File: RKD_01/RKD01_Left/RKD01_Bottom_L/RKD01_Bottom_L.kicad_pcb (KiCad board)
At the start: 2 copper layers, 164.3 x 126.2 mm, 8 parts

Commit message: 寸法を見直し
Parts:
- M1, M2, M3, M4, M5, M6, M7, M8: renamed from Ref**; value Val** -> Mark
- moved M7 21.4 mm to (26.2, 140.5)
- moved M8 4.76 mm to (185.7, 140.5)
- moved M2 4.76 mm to (185.7, 23.8)
- moved M4 2.38 mm to (135.7, 47.6)
- moved M6 2.38 mm to (135.7, 104.8)
- moved M3 2.38 mm to (31.0, 47.6)
- moved M5 2.38 mm to (73.8, 85.7)
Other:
- board size 164.3 x 126.2 mm -> 169.1 x 126.2 mm
- board text added: "RKD01_Left v1.0"
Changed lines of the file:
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@@
 			(drillshape 0)
 			(scaleselection 1)
-			(outputdirectory "../../../../Order/20241231/RKD01/Bottom_L/")
+			(outputdirectory "../../../../Order/20241231/RKD01/Assemble_L/")
 		)
 	)
@@
 	(footprint "kbd_Hole:m2_Screw_Hole"
 		(layer "F.Cu")
-		(at 133.35 104.775)
+		(at 135.7313 104.775)
 		(descr "Mounting Hole 2.2mm, no annular, M2")
 		(tags "mounting hole 2.2mm no annular m2")
-		(property "Reference" "Ref**"
+		(property "Reference" "M6"
 			(at 0 -3.2 0)
 			(layer "F.Fab")
@@
 			)
 		)
-		(property "Value" "Val**"
+		(property "Value" "Mark"
 			(at 0 3.2 0)
 			(layer "F.Fab")
@@
 			)
 		)
+		(sheetname "ルート")
+		(sheetfile "RKD01_Assemble_L.kicad_sch")
 		(attr exclude_from_pos_files exclude_from_bom)
 		(fp_circle
@@
 	(footprint "kbd_Hole:m2_Screw_Hole"
 		(layer "F.Cu")
-		(at 71.4375 85.725)
+		(at 73.8188 85.725)
 		(descr "Mounting Hole 2.2mm, no annular, M2")
 		(tags "mounting hole 2.2mm no annular m2")
-		(property "Reference" "Ref**"
+		(property "Reference" "M5"
 			(at 0 -3.2 0)
 			(layer "F.Fab")
@@
 			)
 		)
-		(property "Value" "Val**"
+		(property "Value" "Mark"
 			(at 0 3.2 0)
 			(layer "F.Fab")
@@
 			)
 		)
+		(sheetname "ルート")
+		(sheetfile "RKD01_Assemble_L.kicad_sch")
 		(attr exclude_from_pos_files exclude_from_bom)
 		(fp_circle
@@
 	(footprint "kbd_Hole:m2_Screw_Hole"
 		(layer "F.Cu")
-		(at 180.975 23.8125)
+		(at 185.7375 23.8125)
 		(descr "Mounting Hole 2.2mm, no annular, M2")
 		(tags "mounting hole 2.2mm no annular m2")
-		(property "Reference" "Ref**"
+		(property "Reference" "M2"
 			(at 0 -3.2 0)
 			(layer "F.Fab")
@@
 			)
 		)
-		(property "Value" "Val**"
+		(property "Value" "Mark"
 			(at 0 3.2 0)
 			(layer "F.Fab")
@@
 			)
 		)
+		(sheetname "ルート")
+		(sheetfile "RKD01_Assemble_L.kicad_sch")
 		(attr exclude_from_pos_files exclude_from_bom)
 		(fp_circle
@@
 	(footprint "kbd_Hole:m2_Screw_Hole"
 		(layer "F.Cu")
-		(at 180.975 140.49375)
+		(at 185.7375 140.4937)
 		(descr "Mounting Hole 2.2mm, no annular, M2")
 		(tags "mounting hole 2.2mm no annular m2")
-		(property "Reference" "Ref**"
+		(property "Reference" "M8"
 			(at 0 -3.2 0)
 			(layer "F.Fab")
@@
 			)
 		)
-		(property "Value" "Val**"
+		(property "Value" "Mark"
 			(at 0 3.2 0)
 			(layer "F.Fab")
@@
 			)
 		)
+		(sheetname "ルート")
+		(sheetfile "RKD01_Assemble_L.kicad_sch")
 		(attr exclude_from_pos_files exclude_from_bom)
 		(fp_circle
@@
 	(footprint "kbd_Hole:m2_Screw_Hole"
 		(layer "F.Cu")
-		(at 47.625 140.49375)
+		(at 26.1938 140.4937)
 		(descr "Mounting Hole 2.2mm, no annular, M2")
 		(tags "mounting hole 2.2mm no annular m2")
-		(property "Reference" "Ref**"
+		(property "Reference" "M7"
 			(at 0 -3.2 0)
 			(layer "F.Fab")
@@
 			)
 		)
-		(property "Value" "Val**"
+		(property "Value" "Mark"
 			(at 0 3.2 0)
 			(layer "F.Fab")
@@
 			)
 		)
+		(sheetname "ルート")
+		(sheetfile "RKD01_Assemble_L.kicad_sch")
 		(attr exclude_from_pos_files exclude_from_bom)
 		(fp_circle
@@
 	(footprint "kbd_Hole:m2_Screw_Hole"
 		(layer "F.Cu")
-		(at 88.10625 23.8125)
+		(at 88.1063 23.8125)
 		(descr "Mounting Hole 2.2mm, no annular, M2")
 		(tags "mounting hole 2.2mm no annular m2")
-		(property "Reference" "Ref**"
+		(property "Reference" "M1"
 			(at 0 -3.2 0)
 			(layer "F.Fab")
@@
 			)
 		)
-		(property "Value" "Val**"
+		(property "Value" "Mark"
 			(at 0 3.2 0)
 			(layer "F.Fab")
@@
 			)
 		)
+		(sheetname "ルート")
+		(sheetfile "RKD01_Assemble_L.kicad_sch")
 		(attr exclude_from_pos_files exclude_from_bom)
 		(fp_circle
@@
 	(footprint "kbd_Hole:m2_Screw_Hole"
 		(layer "F.Cu")
-		(at 133.35 47.625)
+		(at 135.7313 47.625)
 		(descr "Mounting Hole 2.2mm, no annular, M2")
 		(tags "mounting hole 2.2mm no annular m2")
-		(property "Reference" "Ref**"
+		(property "Reference" "M4"
 			(at 0 -3.2 0)
 			(layer "F.Fab")
@@
 			)
 		)
-		(property "Value" "Val**"
+		(property "Value" "Mark"
 			(at 0 3.2 0)
 			(layer "F.Fab")
@@
 			)
 		)
+		(sheetname "ルート")
+		(sheetfile "RKD01_Assemble_L.kicad_sch")
 		(attr exclude_from_pos_files exclude_from_bom)
 		(fp_circle
@@
 	(footprint "kbd_Hole:m2_Screw_Hole"
 		(layer "F.Cu")
-		(at 28.575 47.625)
+		(at 30.9563 47.625)
 		(descr "Mounting Hole 2.2mm, no annular, M2")
 		(tags "mounting hole 2.2mm no annular m2")
-		(property "Reference" "Ref**"
+		(property "Reference" "M3"
 			(at 0 -3.2 0)
 			(layer "F.Fab")
@@
 			)
 		)
-		(property "Value" "Val**"
+		(property "Value" "Mark"
 			(at 0 3.2 0)
 			(layer "F.Fab")
@@
 			)
 		)
+		(sheetname "ルート")
+		(sheetfile "RKD01_Assemble_L.kicad_sch")
 		(attr exclude_from_pos_files exclude_from_bom)
 		(fp_circle
@@
 	)
 	(gr_arc
-		(start 183.35625 19.05)
-		(mid 185.040048 19.747452)
-		(end 185.7375 21.43125)
+		(start 188.1188 19.04995)
+		(mid 189.802583 19.747417)
+		(end 190.50005 21.4312)
 		(stroke
 			(width 0.05)
@@
 	)
 	(gr_line
-		(start 183.35625 19.05)
+		(start 188.1188 19.04995)
 		(end 23.8125 19.05)
 		(stroke
@@
 	)
 	(gr_arc
-		(start 21.43125 21.43125)
-		(mid 22.128702 19.747452)
-		(end 23.8125 19.05)
+		(start 21.43125 21.4313)
+		(mid 22.128702 19.747502)
+		(end 23.8125 19.05005)
 		(stroke
 			(width 0.05)
@@
 	)
 	(gr_arc
-		(start 185.7375 142.875)
-		(mid 185.040048 144.558798)
-		(end 183.35625 145.25625)
+		(start 190.50005 142.875)
+		(mid 189.802601 144.558816)
+		(end 188.1188 145.25625)
 		(stroke
 			(width 0.05)
@@
 	(gr_line
 		(start 23.8125 145.25625)
-		(end 183.35625 145.25625)
+		(end 188.1188 145.25625)
 		(stroke
 			(width 0.05)
@@
 	)
 	(gr_line
-		(start 185.7375 142.875)
-		(end 185.7375 21.43125)
+		(start 190.5 142.875)
+		(end 190.5 21.43125)
 		(stroke
 			(width 0.05)
@@
 		(layer "Edge.Cuts")
 	)
+	(gr_text "RKD01_Left v1.0"
+		(at 176.2125 23.8125 0)
+		(layer "B.SilkS")
+		(effects
+			(font
+				(size 1 1)
+				(thickness 0.1)
+			)
+			(justify left bottom mirror)
+		)
+	)
 )

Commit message: デザイン見直し
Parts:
- removed M7, M8: Mark, kbd_Hole:m2_Screw_Hole
- moved M4 109.0 mm to (192.9, 140.5)
- moved M3 93.0 mm to (26.2, 140.5)
- moved M6 89.6 mm to (78.6, 35.7)
- moved M5 59.7 mm to (78.6, 26.2)
- moved M2 7.14 mm to (192.9, 23.8)
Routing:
- net Row4: track 0.00 -> 2.03 mm
- net Net-(D5-A): track 0.00 -> 2.03 mm
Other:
- board size 169.1 x 126.2 mm -> 176.2 x 126.2 mm

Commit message: デザイン見直し
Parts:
- added M7: Mark, kbd_Hole:m2_Screw_Hole, F.Cu at (23.8, 47.6)
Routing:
- net Row4: track 2.03 -> 0.00 mm
- net Net-(D5-A): track 2.03 -> 0.00 mm
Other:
- outline, holes or cut-outs redrawn
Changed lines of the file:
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@@
 	)
 	(net 0 "")
-	(net 1 "Row4")
-	(net 2 "Net-(D5-A)")
 	(footprint "kbd_Hole:m2_Screw_Hole"
 		(layer "F.Cu")
@@
 	(footprint "kbd_Hole:m2_Screw_Hole"
 		(layer "F.Cu")
+		(at 23.8125 47.625)
+		(descr "Mounting Hole 2.2mm, no annular, M2")
+		(tags "mounting hole 2.2mm no annular m2")
+		(property "Reference" "M7"
+			(at 0 -3.2 0)
+			(layer "F.Fab")
+			(effects
+				(font
+					(size 1 1)
+					(thickness 0.15)
+				)
+			)
+		)
+		(property "Value" "Mark"
+			(at 0 3.2 0)
+			(layer "F.Fab")
+			(effects
+				(font
+					(size 1 1)
+					(thickness 0.15)
+				)
+			)
+		)
+		(property "Footprint" "kbd_Hole:m2_Screw_Hole"
+			(at 0 0 0)
+			(layer "F.Fab")
+			(hide yes)
+			(effects
+				(font
+					(size 1.27 1.27)
+					(thickness 0.15)
+				)
+			)
+		)
+		(property "Datasheet" ""
+			(at 0 0 0)
+			(layer "F.Fab")
+			(hide yes)
+			(effects
+				(font
+					(size 1.27 1.27)
+					(thickness 0.15)
+				)
+			)
+		)
+		(property "Description" ""
+			(at 0 0 0)
+			(layer "F.Fab")
+			(hide yes)
+			(effects
+				(font
+					(size 1.27 1.27)
+					(thickness 0.15)
+				)
+			)
+		)
+		(attr exclude_from_pos_files)
+		(fp_circle
+			(center 0 0)
+			(end 2.2 0)
+			(stroke
+				(width 0.15)
+				(type solid)
+			)
+			(fill none)
+			(layer "Cmts.User")
+		)
+		(fp_circle
+			(center 0 0)
+			(end 2.45 0)
+			(stroke
+				(width 0.05)
+				(type solid)
+			)
+			(fill none)
+			(layer "F.CrtYd")
+		)
+		(fp_text user "${REFERENCE}"
+			(at 0.3 0 0)
+			(layer "F.Fab")
+			(effects
+				(font
+					(size 1 1)
+					(thickness 0.15)
+				)
+			)
+		)
+		(pad "" np_thru_hole circle
+			(at 0 0)
+			(size 2.2 2.2)
+			(drill 2.2)
+			(layers "*.Cu" "*.Mask")
+		)
+	)
+	(footprint "kbd_Hole:m2_Screw_Hole"
+		(layer "F.Cu")
 		(at 26.1938 140.4937)
 		(descr "Mounting Hole 2.2mm, no annular, M2")
@@
 		)
 	)
-	(gr_arc
-		(start 195.26255 19.0499)
-		(mid 196.946319 19.747381)
-		(end 197.6438 21.43115)
+	(gr_line
+		(start 196.453125 19.05)
+		(end 22.621875 19.05)
 		(stroke
 			(width 0.05)
@@
 		(layer "Edge.Cuts")
 	)
-	(gr_line
-		(start 195.26255 19.0499)
-		(end 23.81245 19.05005)
+	(gr_arc
+		(start 22.621875 145.25625)
+		(mid 21.779976 144.907524)
+		(end 21.43125 144.065625)
 		(stroke
 			(width 0.05)
@@
 	)
 	(gr_arc
-		(start 21.4312 21.4313)
-		(mid 22.128652 19.747502)
-		(end 23.81245 19.05005)
+		(start 196.453125 19.05)
+		(mid 197.295024 19.398726)
+		(end 197.64375 20.240625)
 		(stroke
 			(width 0.05)
@@
 	)
 	(gr_arc
-		(start 197.6437 142.875)
-		(mid 196.946248 144.558798)
-		(end 195.26245 145.25625)
+		(start 197.64375 144.065625)
+		(mid 197.295024 144.907524)
+		(end 196.453125 145.25625)
 		(stroke
 			(width 0.05)
@@
 	)
 	(gr_arc
-		(start 23.8125 145.25625)
-		(mid 22.128702 144.558798)
-		(end 21.43125 142.875)
+		(start 21.43125 20.240625)
+		(mid 21.779976 19.398726)
+		(end 22.621875 19.05)
 		(stroke
 			(width 0.05)
@@
 	)
 	(gr_line
-		(start 23.8125 145.25625)
-		(end 195.26245 145.25625)
+		(start 22.621875 145.25625)
+		(end 196.453125 145.25625)
 		(stroke
 			(width 0.05)
@@
 	)
 	(gr_line
-		(start 197.6437 142.875)
-		(end 197.6437 21.43125)
+		(start 197.64375 144.065625)
+		(end 197.64375 20.240625)
 		(stroke
 			(width 0.05)
@@
 	)
 	(gr_line
-		(start 21.43125 142.875)
-		(end 21.43125 21.43125)
+		(start 21.43125 144.065625)
+		(end 21.43125 20.240625)
 		(stroke
 			(width 0.05)
@@
 		)
 	)
-	(segment
-		(start 33.3376 126.8125)
-		(end 33.3376 124.7775)
-		(width 0.25)
-		(layer "B.Cu")
-		(net 1)
-	)
-	(segment
-		(start 33.3376 132.3975)
-		(end 33.3376 130.3625)
-		(width 0.25)
-		(layer "B.Cu")
-		(net 2)
-	)
 )

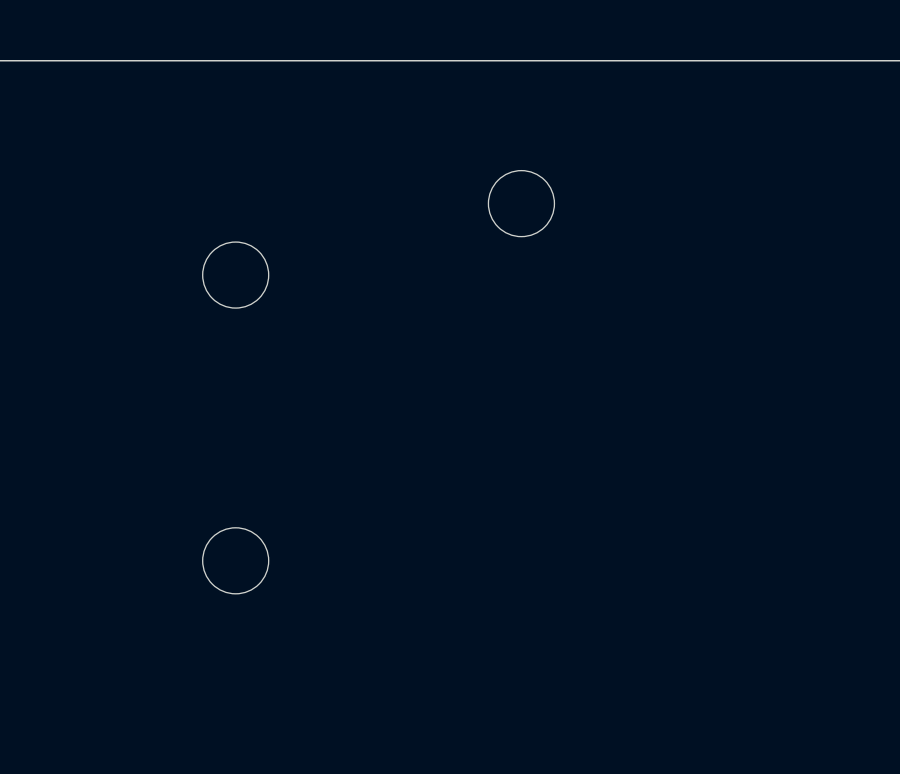
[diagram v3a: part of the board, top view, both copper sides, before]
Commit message: promicro部分拡張
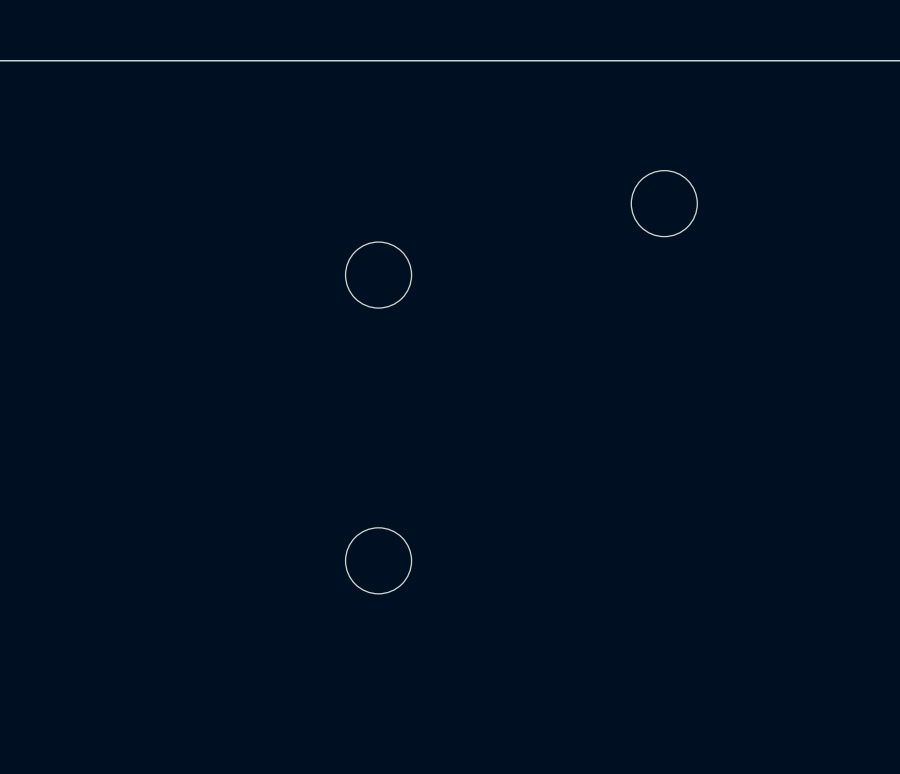
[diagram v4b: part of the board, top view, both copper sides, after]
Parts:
- moved M1 4.76 mm to (92.9, 23.8)
- moved M5 4.76 mm to (83.3, 26.2)
- moved M6 4.76 mm to (83.3, 35.7)
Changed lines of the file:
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@@
 	(footprint "kbd_Hole:m2_Screw_Hole"
 		(layer "F.Cu")
-		(at 78.5813 26.1937)
+		(at 83.34375 26.1937)
 		(descr "Mounting Hole 2.2mm, no annular, M2")
 		(tags "mounting hole 2.2mm no annular m2")
@@
 	(footprint "kbd_Hole:m2_Screw_Hole"
 		(layer "F.Cu")
-		(at 78.5813 35.7187)
+		(at 83.34375 35.7187)
 		(descr "Mounting Hole 2.2mm, no annular, M2")
 		(tags "mounting hole 2.2mm no annular m2")
@@
 	(footprint "kbd_Hole:m2_Screw_Hole"
 		(layer "F.Cu")
-		(at 88.1063 23.8125)
-		(descr "Mounting Hole 2.2mm, no annular, M2")
-		(tags "mounting hole 2.2mm no annular m2")
+		(at 92.86875 23.8125)
+		(descr "Mounting Hole 2.2mm, no annular, M2")
+		(tags "mounting hole 2.2mm no annular m2")

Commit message: SU120用の穴あけ
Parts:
- added M8: Mark, kbd_Hole:m2_Screw_Hole, F.Cu at (59.5, 23.8)
- added M9: Mark, kbd_Hole:m2_Screw_Hole, F.Cu at (59.5, 38.1)
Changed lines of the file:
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@@
+	(footprint "kbd_Hole:m2_Screw_Hole"
+		(layer "F.Cu")
+		(at 59.53125 38.1)
+		(descr "Mounting Hole 2.2mm, no annular, M2")
+		(tags "mounting hole 2.2mm no annular m2")
+		(property "Reference" "M9"
+			(at 0 -3.2 0)
+			(layer "F.Fab")
+			(effects
+				(font
+					(size 1 1)
+					(thickness 0.15)
+				)
+			)
+		)
+		(property "Value" "Mark"
+			(at 0 3.2 0)
+			(layer "F.Fab")
+			(effects
+				(font
+					(size 1 1)
+					(thickness 0.15)
+				)
+			)
+		)
+		(property "Footprint" "kbd_Hole:m2_Screw_Hole"
+			(at 0 0 0)
+			(layer "F.Fab")
+			(hide yes)
+			(effects
+				(font
+					(size 1.27 1.27)
+					(thickness 0.15)
+				)
+			)
+		)
+		(property "Datasheet" ""
+			(at 0 0 0)
+			(layer "F.Fab")
+			(hide yes)
+			(effects
+				(font
+					(size 1.27 1.27)
+					(thickness 0.15)
+				)
+			)
+		)
+		(property "Description" ""
+			(at 0 0 0)
+			(layer "F.Fab")
+			(hide yes)
+			(effects
+				(font
+					(size 1.27 1.27)
+					(thickness 0.15)
+				)
+			)
+		)
+		(attr exclude_from_pos_files)
+		(fp_circle
+			(center 0 0)
+			(end 2.2 0)
+			(stroke
+				(width 0.15)
+				(type solid)
+			)
+			(fill none)
+			(layer "Cmts.User")
+		)
+		(fp_circle
+			(center 0 0)
+			(end 2.45 0)
+			(stroke
+				(width 0.05)
+				(type solid)
+			)
+			(fill none)
+			(layer "F.CrtYd")
+		)
+		(fp_text user "${REFERENCE}"
+			(at 0.3 0 0)
+			(layer "F.Fab")
+			(effects
+				(font
+					(size 1 1)
+					(thickness 0.15)
+				)
+			)
+		)
+		(pad "" np_thru_hole circle
+			(at 0 0)
+			(size 2.2 2.2)
+			(drill 2.2)
+			(layers "*.Cu" "*.Mask")
+		)
+	)
 	(footprint "kbd_Hole:m2_Screw_Hole"
 		(layer "F.Cu")
@@
 	(footprint "kbd_Hole:m2_Screw_Hole"
 		(layer "F.Cu")
+		(at 59.53125 23.8125)
+		(descr "Mounting Hole 2.2mm, no annular, M2")
+		(tags "mounting hole 2.2mm no annular m2")
+		(property "Reference" "M8"
+			(at 0 -3.2 0)
+			(layer "F.Fab")
+			(effects
+				(font
+					(size 1 1)
+					(thickness 0.15)
+				)
+			)
+		)
+		(property "Value" "Mark"
+			(at 0 3.2 0)
+			(layer "F.Fab")
+			(effects
+				(font
+					(size 1 1)
+					(thickness 0.15)
+				)
+			)
+		)
+		(property "Footprint" "kbd_Hole:m2_Screw_Hole"
+			(at 0 0 0)
+			(layer "F.Fab")
+			(hide yes)
+			(effects
+				(font
+					(size 1.27 1.27)
+					(thickness 0.15)
+				)
+			)
+		)
+		(property "Datasheet" ""
+			(at 0 0 0)
+			(layer "F.Fab")
+			(hide yes)
+			(effects
+				(font
+					(size 1.27 1.27)
+					(thickness 0.15)
+				)
+			)
+		)
+		(property "Description" ""
+			(at 0 0 0)
+			(layer "F.Fab")
+			(hide yes)
+			(effects
+				(font
+					(size 1.27 1.27)
+					(thickness 0.15)
+				)
+			)
+		)
+		(attr exclude_from_pos_files)
+		(fp_circle
+			(center 0 0)
+			(end 2.2 0)
+			(stroke
+				(width 0.15)
+				(type solid)
+			)
+			(fill none)
+			(layer "Cmts.User")
+		)
+		(fp_circle
+			(center 0 0)
+			(end 2.45 0)
+			(stroke
+				(width 0.05)
+				(type solid)
+			)
+			(fill none)
+			(layer "F.CrtYd")
+		)
+		(fp_text user "${REFERENCE}"
+			(at 0.3 0 0)
+			(layer "F.Fab")
+			(effects
+				(font
+					(size 1 1)
+					(thickness 0.15)
+				)
+			)
+		)
+		(pad "" np_thru_hole circle
+			(at 0 0)
+			(size 2.2 2.2)
+			(drill 2.2)
+			(layers "*.Cu" "*.Mask")
+		)
+	)
+	(footprint "kbd_Hole:m2_Screw_Hole"
+		(layer "F.Cu")
 		(at 26.1938 140.4937)
 		(descr "Mounting Hole 2.2mm, no annular, M2")
@@
 	)
 	(gr_line
+		(start 21.43125 30.95625)
+		(end 59.53125 30.95625)
+		(stroke
+			(width 0.1)
+			(type default)
+		)
+		(layer "Cmts.User")
+	)
+	(gr_line
+		(start 59.53125 19.05)
+		(end 59.53125 23.8125)
+		(stroke
+			(width 0.1)
+			(type default)
+		)
+		(layer "Cmts.User")
+	)
+	(gr_line
+		(start 59.53125 23.8125)
+		(end 59.53125 38.1)
+		(stroke
+			(width 0.1)
+			(type default)
+		)
+		(layer "Cmts.User")
+	)
+	(gr_line
